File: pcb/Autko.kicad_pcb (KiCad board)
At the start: 2 copper layers, 140 x 155 mm, 123 parts, among them J1 PDI, M1 LEFT, M2 RIGHT, Q1 Si4368DY, Q2 BC817, SW1 POWER, SW2 START, SW3 STOP, U1 LTC3872, U10 CNY70, U11 TB6612FNG, U12 RN4678, U2 TLV1117-33, U3 ATxmega16A4U-A, U4 CNY70, U5 CNY70, U6 CNY70, U7 CNY70, U8 CNY70, U9 CNY70, Y1 8MHz

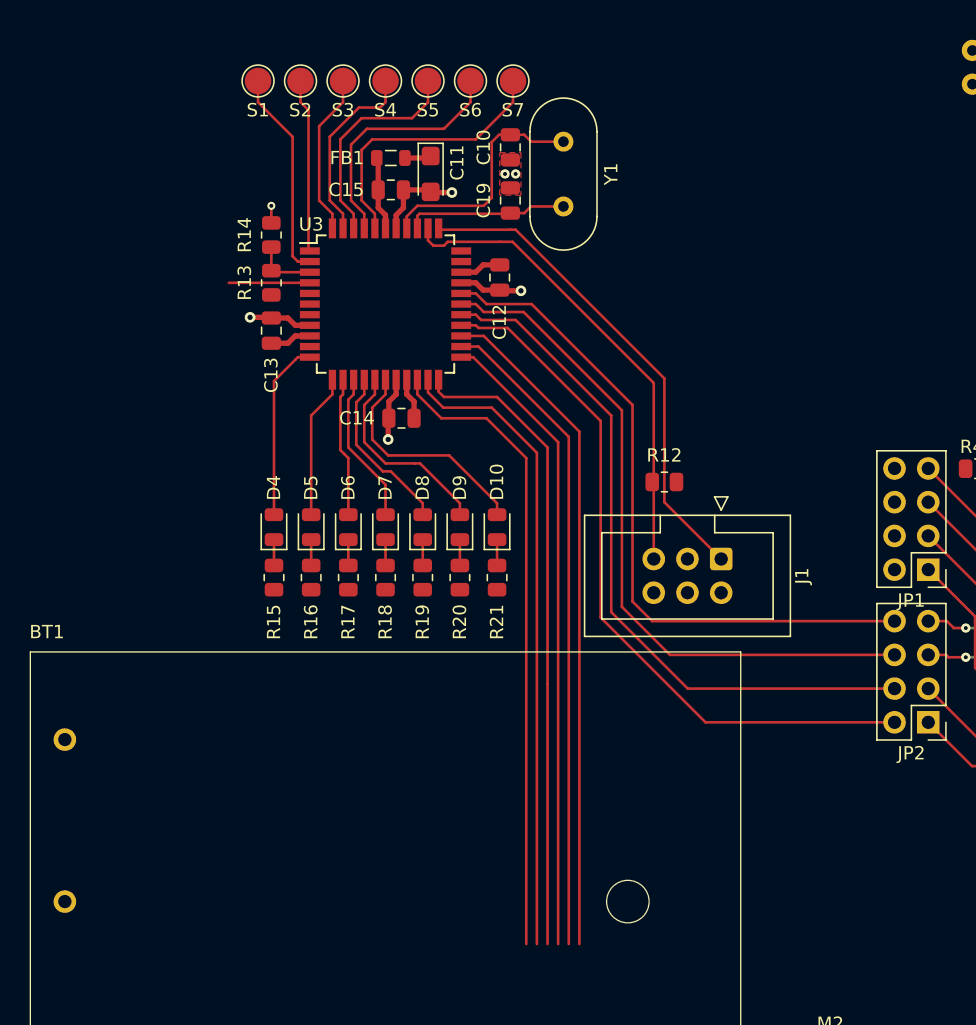
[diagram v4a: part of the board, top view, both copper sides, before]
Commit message: [pcb] Rotate uC by 45 deg
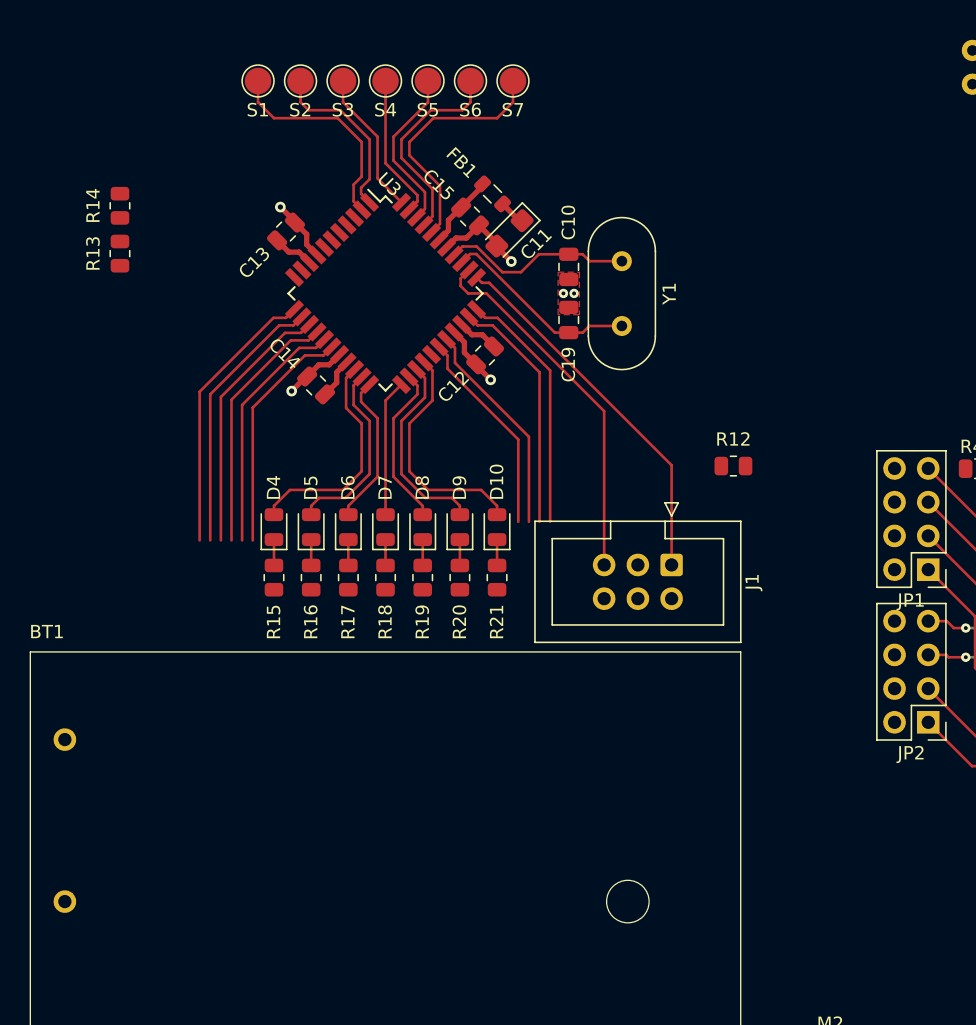
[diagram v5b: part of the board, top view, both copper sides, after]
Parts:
- moved R14 11.6 mm to (79.5, 71.9)
- moved R13 11.6 mm to (79.5, 75.5)
- moved C10 10.0 mm to (113.3, 76.5)
- moved C19 10.0 mm to (113.3, 80.5)
- moved Y1 10.0 mm to (117.3, 81.0)
- moved FB1 8.12 mm to (107.6, 71.0), turned to -45 degrees
- moved C13 7.55 mm to (92.0, 73.8), turned to 45 degrees
- moved C11 7.43 mm to (108.8, 74.0), turned to -135 degrees
- moved C14 6.89 mm to (94.3, 85.4), turned to 135 degrees
- moved C15 6.29 mm to (105.9, 72.7), turned to -45 degrees
- moved C12 5.97 mm to (107.0, 83.2), turned to -135 degrees
- moved R12 5.34 mm to (125.7, 91.5)
- moved J1 3.76 mm to (121.0, 98.9)
- moved U3 0.80 mm to (99.5, 78.5), turned to -45 degrees
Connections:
- U3 pad 11: /Microcontroller/LED1 -> unconnected-(U3-PC1-Pad11)
- U3 pad 12: /Microcontroller/LED2 -> /Microcontroller/M1_PWM
- U3 pad 13: /Microcontroller/LED3 -> /Microcontroller/M1_IN2
- U3 pad 14: /Microcontroller/LED4 -> /Microcontroller/M1_IN1
- U3 pad 15: /Microcontroller/LED5 -> /Microcontroller/M2_IN1
- U3 pad 16: /Microcontroller/LED6 -> /Microcontroller/M2_IN2
- U3 pad 17: /Microcontroller/LED7 -> /Microcontroller/M2_PWM
- U3 pad 20: /Microcontroller/M1_PWM -> /Microcontroller/LED1
- U3 pad 21: /Microcontroller/M1_IN2 -> /Microcontroller/LED2
- U3 pad 22: /Microcontroller/M1_IN1 -> /Microcontroller/LED3
- U3 pad 23: /Microcontroller/M2_IN1 -> /Microcontroller/LED4
- U3 pad 24: /Microcontroller/M2_IN2 -> /Microcontroller/LED5
- U3 pad 25: /Microcontroller/M2_PWM -> /Microcontroller/LED6
- U3 pad 26: /Bluetooth/TX -> /Microcontroller/LED7
- U3 pad 27: /Bluetooth/RX -> unconnected-(U3-PD7-Pad27)
- U3 pad 32: unconnected-(U3-PE2-Pad32) -> /Bluetooth/TX
- U3 pad 33: unconnected-(U3-PE3-Pad33) -> /Bluetooth/RX
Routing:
- net /Bluetooth/RTS: track 52.2 -> 15.6 mm
- net /Bluetooth/TX: track 53.7 -> 18.3 mm
- net /Bluetooth/CTS: track 51.5 -> 16.3 mm
- net /Bluetooth/RX: track 53.0 -> 18.8 mm
- net /Microcontroller/M2_PWM: track 50.5 -> 17.9 mm
- net /Microcontroller/M2_IN2: track 49.1 -> 18.4 mm
- net /Microcontroller/M2_IN1: track 47.8 -> 19.2 mm
- net /Microcontroller/M1_IN1: track 48.2 -> 19.7 mm
- net /Microcontroller/M1_IN2: track 48.0 -> 20.3 mm
- net /Microcontroller/M1_PWM: track 47.9 -> 20.9 mm
- net /Microcontroller/PDI_DATA: track 37.1 -> 28.2 mm
- net /Microcontroller/PDI_CLK: track 35.8 -> 27.8 mm
- net /Line sensors/IR_LEDS_ON: track 6.10 -> 0.00 mm
- net Net-(U3-PA7): track 4.72 -> 0.00 mm
- net /Line sensors/SENSOR5: track 16.5 -> 12.6 mm
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
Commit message: [pcb] Remove unnecessary capacitors
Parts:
- removed C11, C20: 10uF, Capacitor_Tantalum_SMD:CP_EIA-3216-18_Kemet-A
- moved C16 28.2 mm to (108.8, 74.0), turned to -135 degrees
- moved R12 3.94 mm to (122.1, 93.1)

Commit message: [pcb] BT routing
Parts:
- added C25: 100nF, Capacitor_SMD:C_0805_2012Metric, F.Cu at (144.3, 95.5)
- added U12: 74HC14, Package_SO:TSSOP-14_4.4x5mm_P0.65mm, F.Cu at (142.3, 99.5)
- moved R37 18.2 mm to (137.4, 89.1), turned to 90 degrees
- moved R38 13.4 mm to (139.6, 89.1), turned to 90 degrees
- moved R39 12.9 mm to (141.8, 89.1), turned to 90 degrees
- moved JP2 8.84 mm to (132.2, 114.1)
- moved JP1 8.66 mm to (132.2, 102.1)
- moved TP1 3.61 mm to (54.9, 117.7)
- moved R40 2.60 mm to (144.0, 89.1), turned to 90 degrees
- renumbered C12 to C11, C13 to C12, C14 to C13, C15 to C14, C16 to C15, C17 to C16, C18 to C17, C19 to C18, C21 to C19, C22 to C20, C23 to C21, C24 to C22, C25 to C23, C26 to C24, C27 to C26, D12 to D11, R23 to R22, R24 to R23, R25 to R24, R26 to R25, R27 to R26, R28 to R27, R29 to R28, R30 to R29, R31 to R30, R32 to R31, R33 to R32, R34 to R33, R35 to R34, R36 to R35, R37 to R36, R38 to R37, R40 to R38, R41 to R40, R42 to R41, R43 to R42, U12 to U13
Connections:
- JP1 pad 1: /Bluetooth/EAN -> Net-(JP1-Pad1)
- JP1 pad 3: /Bluetooth/P2_4 -> Net-(JP1-Pad3)
- JP1 pad 4: +3.3V -> GND
- JP1 pad 5: /Bluetooth/P2_0 -> Net-(JP1-Pad5)
- JP1 pad 6: +3.3V -> GND
- JP1 pad 7: /Bluetooth/P0_5 -> Net-(JP1-Pad7)
- JP1 pad 8: +3.3V -> GND
- R37 pad 2: /Bluetooth/EAN -> Net-(JP1-Pad1)
- R38 pad 1: /Bluetooth/P2_4 -> +3.3V
- R38 pad 2: GND -> Net-(JP1-Pad3)
- R39 pad 1: /Bluetooth/P2_0 -> +3.3V
- R39 pad 2: GND -> Net-(JP1-Pad5)
- R40 pad 1: /Bluetooth/P0_5 -> +3.3V
- R40 pad 2: GND -> Net-(JP1-Pad7)
- SW2 pad 2: +5V -> +3.3V
- SW3 pad 2: +5V -> +3.3V
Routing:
- net Net-(JP1-Pad7): track 0.00 -> 34.7 mm
- net Net-(JP1-Pad5): track 0.00 -> 33.6 mm
- net /Bluetooth/TX: track 18.3 -> 49.3 mm
- net Net-(JP1-Pad1): track 0.00 -> 31.0 mm
- net /Bluetooth/RTS: track 15.6 -> 45.9 mm, vias 0 -> 2
- net /Bluetooth/CTS: track 16.3 -> 46.0 mm, vias 0 -> 2
- net Net-(JP1-Pad3): track 0.00 -> 29.4 mm
- net /Bluetooth/RX: track 18.8 -> 47.8 mm
- net +3.3V: track 14.9 -> 32.0 mm, vias 0 -> 5
- net /Microcontroller/M2_PWM: track 17.9 -> 30.3 mm
- net /Microcontroller/M2_IN2: track 18.4 -> 30.8 mm
- net /Microcontroller/M2_IN1: track 19.2 -> 31.6 mm
- net /Microcontroller/M1_PWM: track 20.9 -> 33.3 mm
- net /Microcontroller/M1_IN2: track 20.3 -> 32.7 mm
- net /Microcontroller/M1_IN1: track 19.7 -> 32.1 mm
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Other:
- board text added: "Autko 2.0"
- board text added: "EAN"
- board text added: "P0_5"
- board text added: "P2_0"
- board text added: "P2_4"
- board text added: "application"
- board text added: "closed"
- board text added: "command"
- board text added: "data"
- board text added: "mode"
- board text added: "open"
- board text added: "write EEPROM, test"
- board text added: "write FLASH"
- board text added: "© 2023 Kamil Rosiński"

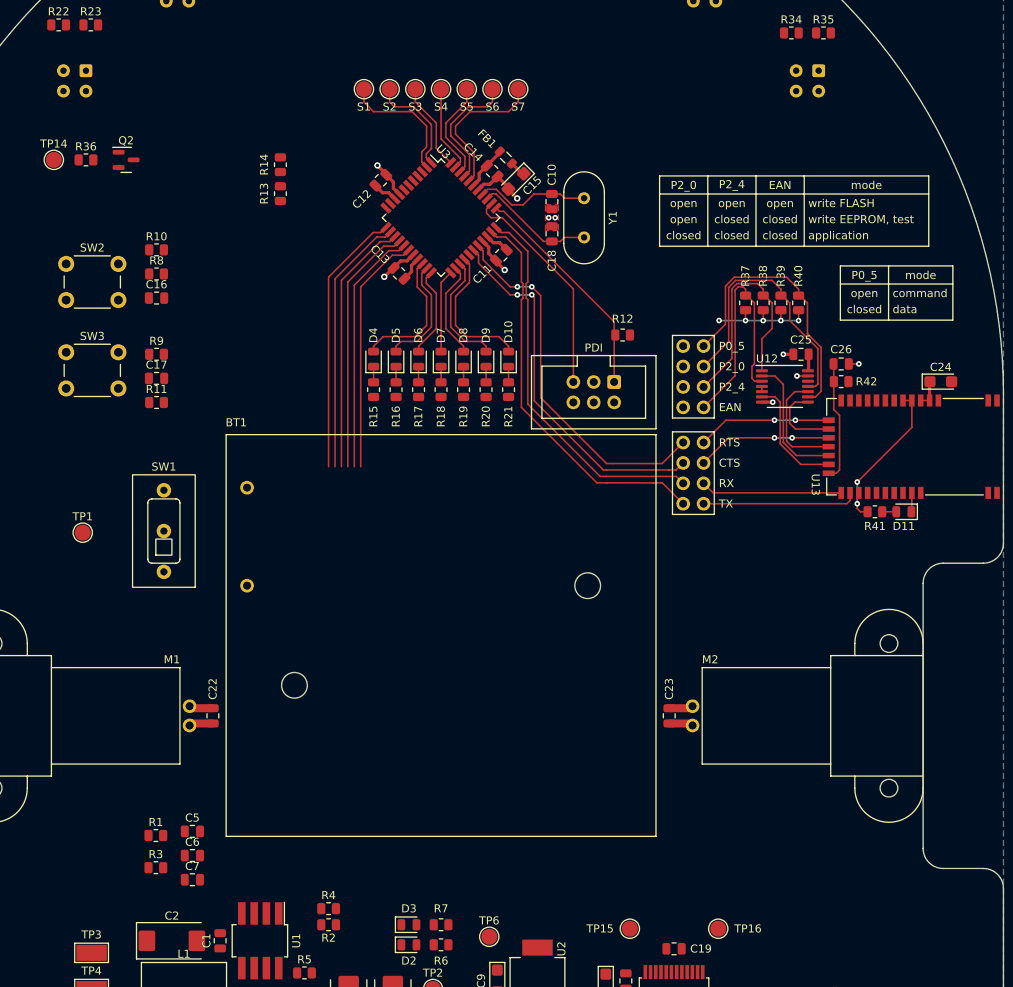
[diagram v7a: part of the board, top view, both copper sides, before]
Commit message: [pcb] Ball caster added to PCB
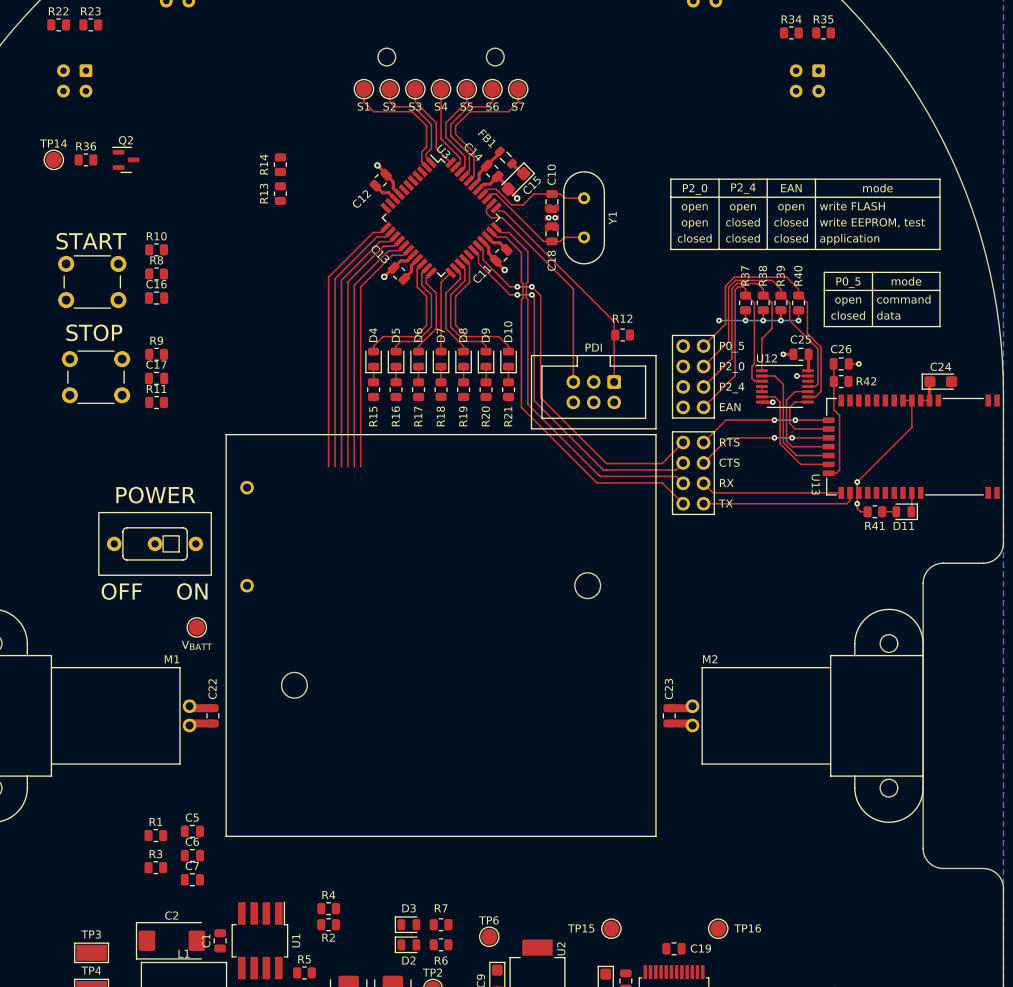
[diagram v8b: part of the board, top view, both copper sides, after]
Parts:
- added REF**: Pololu_ball_caster, Autko:Pololu_ball_caster, F.Cu at (99.5, 58.5)
- moved TP1 18.5 mm to (69.1, 129.5)
- moved TP15 2.30 mm to (120.7, 167.0)
- moved SW1 1.94 mm to (63.9, 119.1), turned to -90 degrees
- moved SW3 0.97 mm to (53.3, 96.1)
